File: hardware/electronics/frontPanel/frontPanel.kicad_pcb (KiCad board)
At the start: 2 copper layers, 104 x 54.6 mm, 9 parts, among them J1 M8S-04PFFR-SF8001, J2 M8S-04PFFR-SF8001, J3 MUSBRM1C1M0, J4 MRJ-5381-M1, J5 M3, J6 M3, J7 M3, J8 M3, J9 LPS28

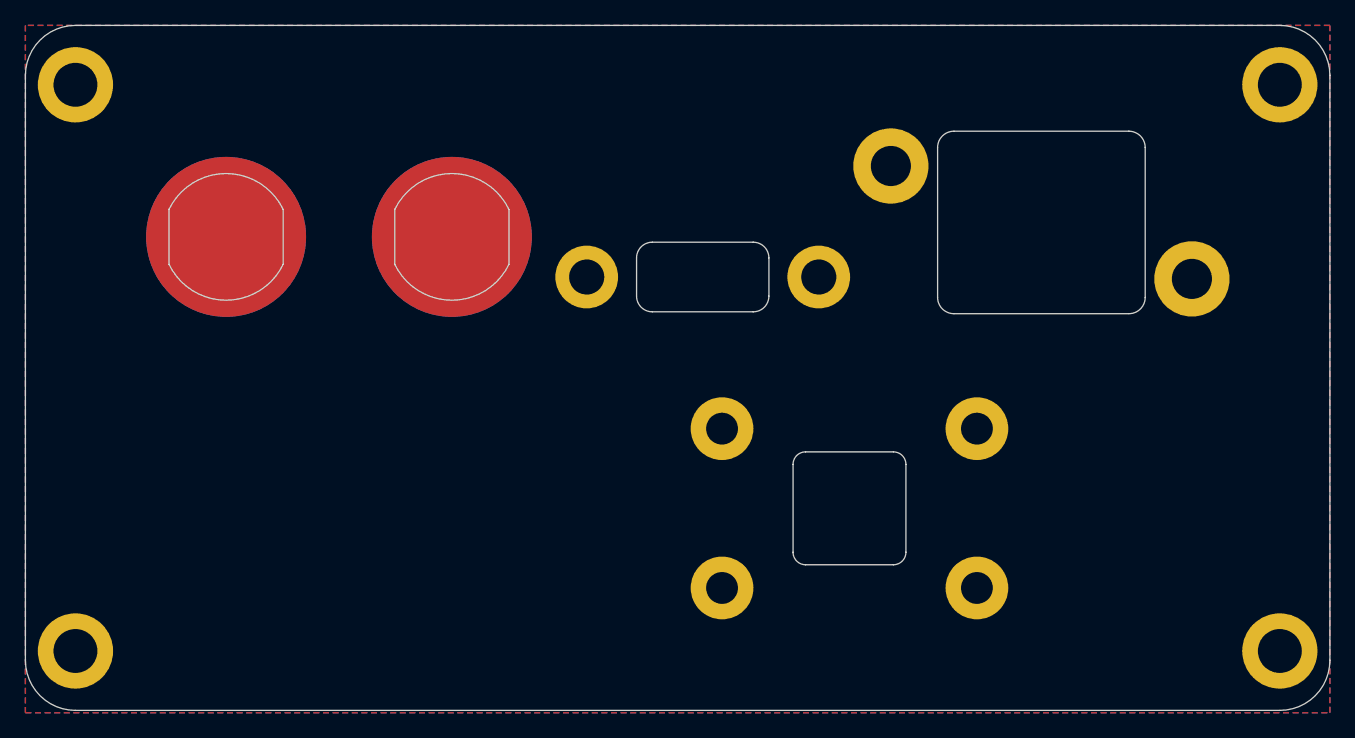
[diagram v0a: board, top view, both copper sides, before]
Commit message: front/back enclosure panels
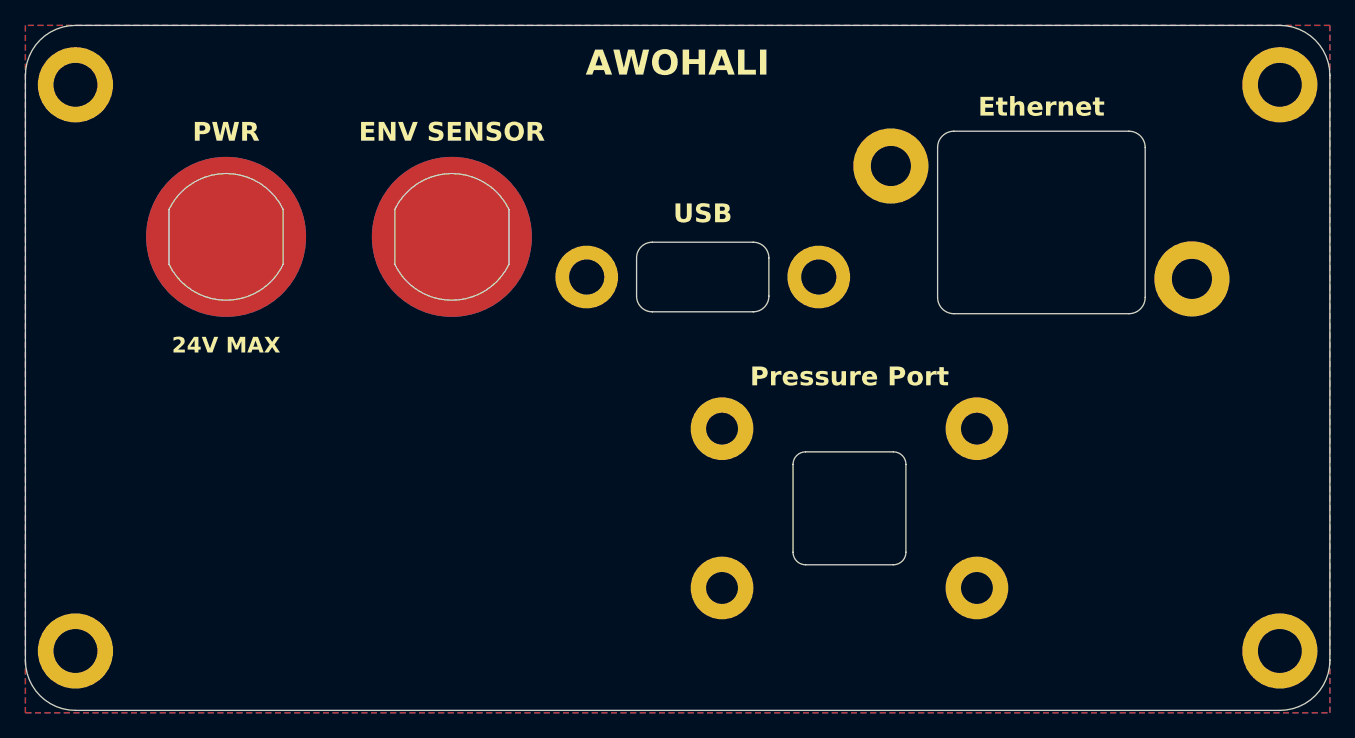
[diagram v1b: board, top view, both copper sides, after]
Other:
- board text added: "24V MAX"
- board text added: "AWOHALI"
- board text added: "ENV SENSOR"
- board text added: "Ethernet"
- board text added: "PWR"
- board text added: "Pressure Port"
- board text added: "USB"
